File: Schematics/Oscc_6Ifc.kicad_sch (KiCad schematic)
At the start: 95 parts, among them J35 Conn_01x10h, J36 Conn_01x10h, J37 Conn_01x12, J38 Conn_01x12, J39 Conn_01x10h, J40 Conn_01x10h, J41 Conn_01x12, J42 Conn_01x12, J43 Conn_01x10h, J44 Conn_01x04, J45 Conn_01x04, J46 Conn_01x12, J47 Conn_01x10h, J48 Conn_01x12, P2 Conn_01x03, U86 LM358, U87 LMT358N, U88 LMT358N, U89 LM358, U90 LM358, U91 LMT358N, U92 LMT358N, U93 LM358, U94 LM358, U95 LMT358N, U96 LM358, U97 LMT358N, U98 LM78L05

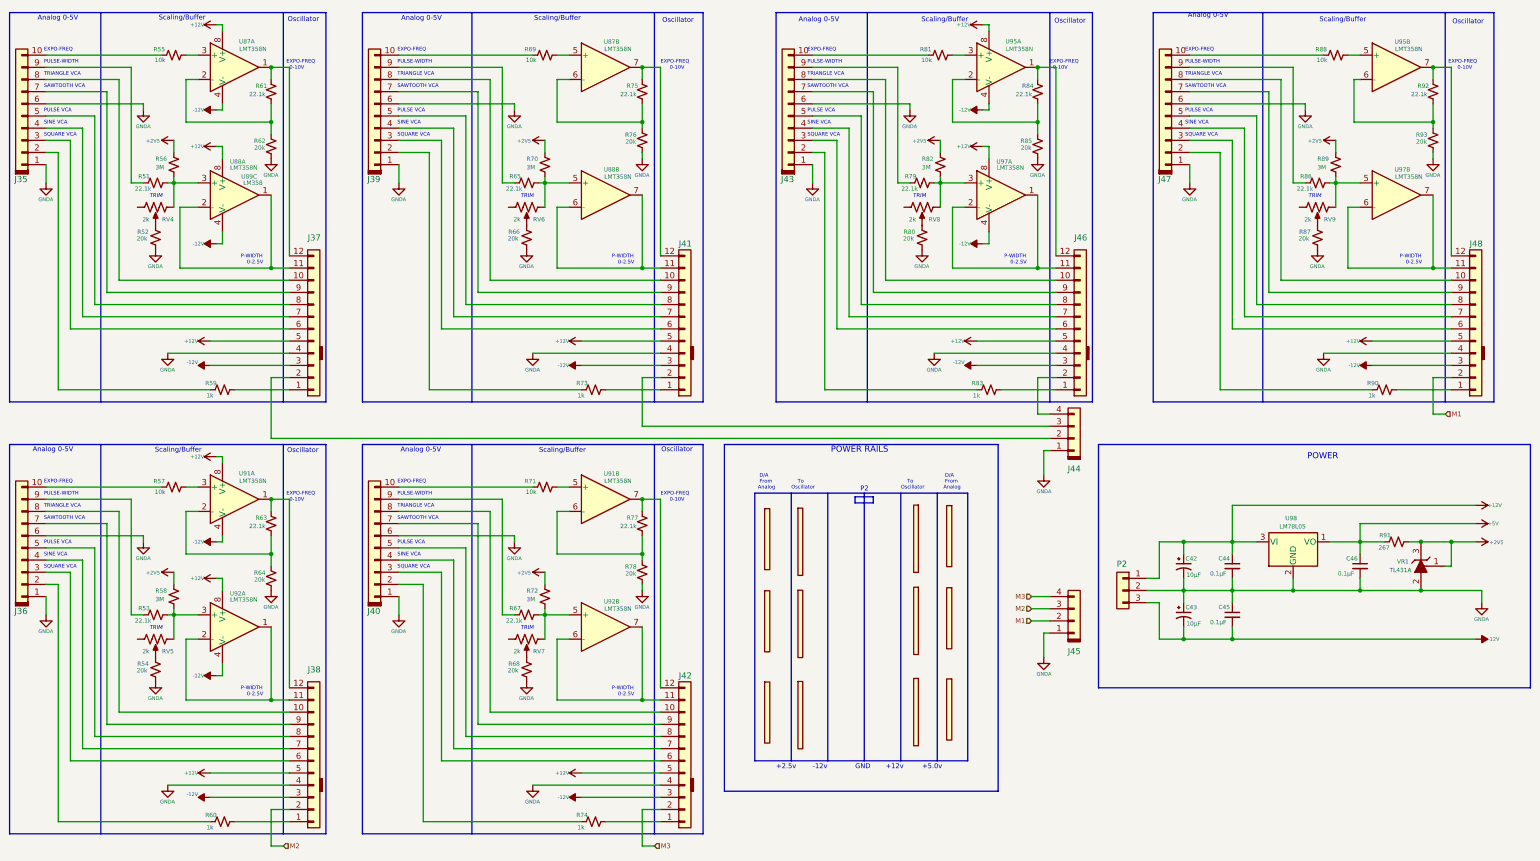
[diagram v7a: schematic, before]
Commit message: Partial software with complete hardware on best 3 state filter with 4 outputs.
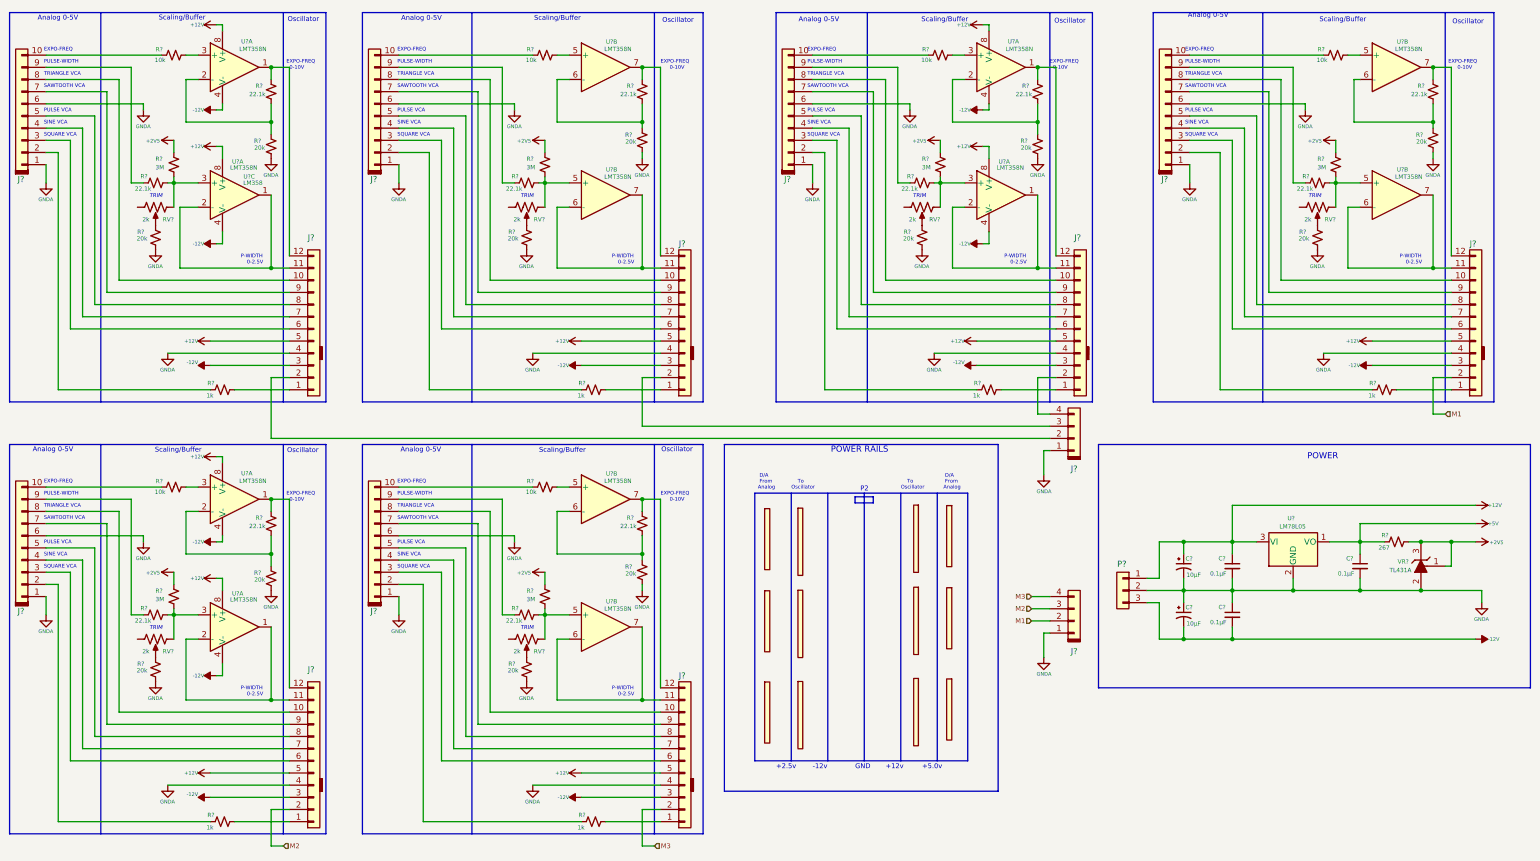
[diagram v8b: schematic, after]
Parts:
- renumbered C42 to C?, C44 to C?, C46 to C?, C45 to C?, C43 to C?, J47 to J?, J46 to J?, J40 to J?, J41 to J?, J44 to J?, J38 to J?, J45 to J?, J39 to J?, J42 to J?, J43 to J?, J35 to J?, J48 to J?, J36 to J?, J37 to J?, JM12 to JM?, JM5 to JM?, JM1 to JM?, JM7 to JM?, JM3 to JM?, JM9 to JM?, JM10 to JM?, JM11 to JM?, JM2 to JM?, JM6 to JM?, JM4 to JM?, JM8 to JM?, P2 to P?, R86 to R?, R85 to R?, R61 to R?, R84 to R?, R81 to R?, R54 to R?, R59 to R?, R82 to R?, R58 to R?, R79 to R?, R57 to R?, R93 to R?, R91 to R?, R74 to R?, R87 to R?, R69 to R?, R70 to R?, R72 to R?, R51 to R?, R89 to R?, R92 to R?, R60 to R?, R53 to R?, R68 to R?, R88 to R?, R55 to R?, R83 to R?, R52 to R?, R66 to R?, R90 to R?, R71 to R?, R73 to R?, R77 to R?, R63 to R?, R62 to R?, R80 to R?, R76 to R?, R75 to R?, R67 to R?, R64 to R?, R78 to R?, R65 to R?, R56 to R?, RV4 to RV?, RV6 to RV?, RV5 to RV?, RV7 to RV?, RV8 to RV?, RV9 to RV?, U97 to U?, U95 to U?, U88 to U?, U89 to U?, U98 to U?, U90 to U?, U92 to U?, U91 to U?, U87 to U?, U93 to U?, U86 to U?, U96 to U?, U94 to U?, VR1 to VR?
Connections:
- net at RV?. (3): now also R?.1 (x3)
